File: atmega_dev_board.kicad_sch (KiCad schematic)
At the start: 40 parts, among them J1 GPIO Header, J2 USB_B_Micro, J3 GPIO Header, J4 ICSP Header, Q1 Q_PMOS_DGS, SW1 SW_Push, U1 LM358, U2 NCV8114ASN330T1G, U3 NCV8114ASN330T1G, U4 ATmega328P-A, U5 CH340G, Y1 Crystal_GND23, Y2 Crystal_GND23

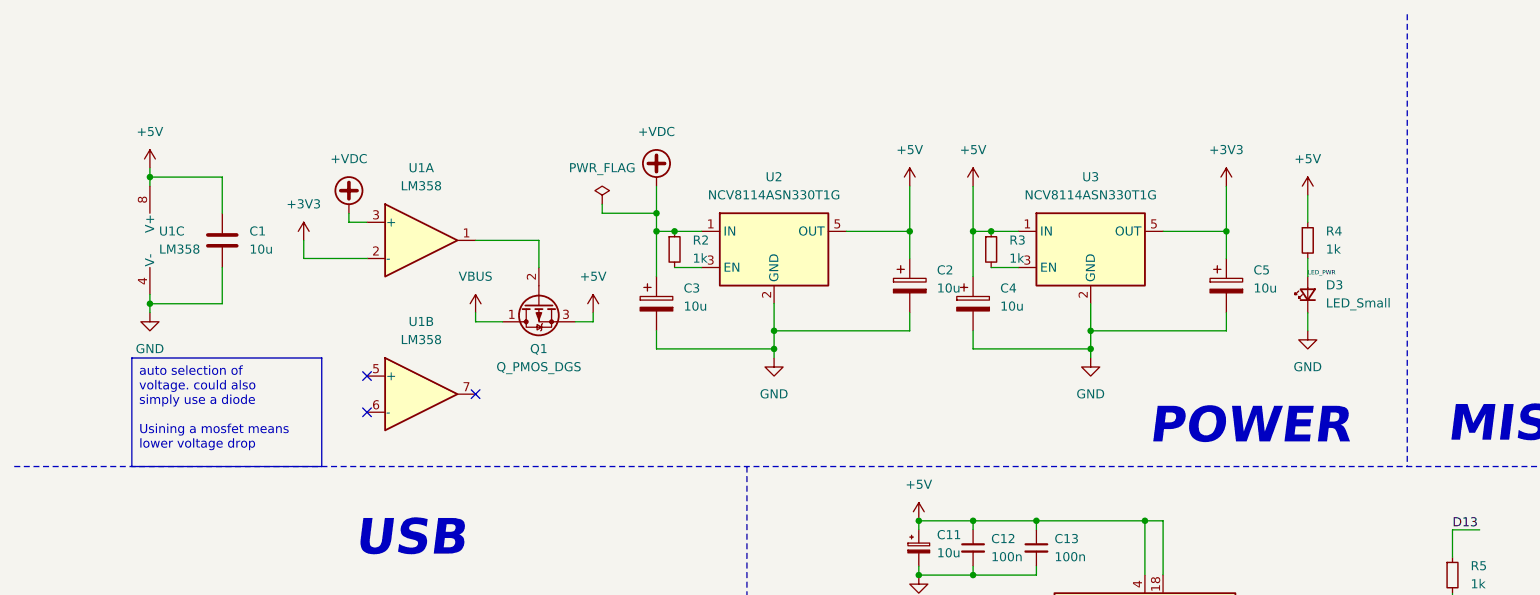
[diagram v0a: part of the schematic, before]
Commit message: Replace op-amps with a diode
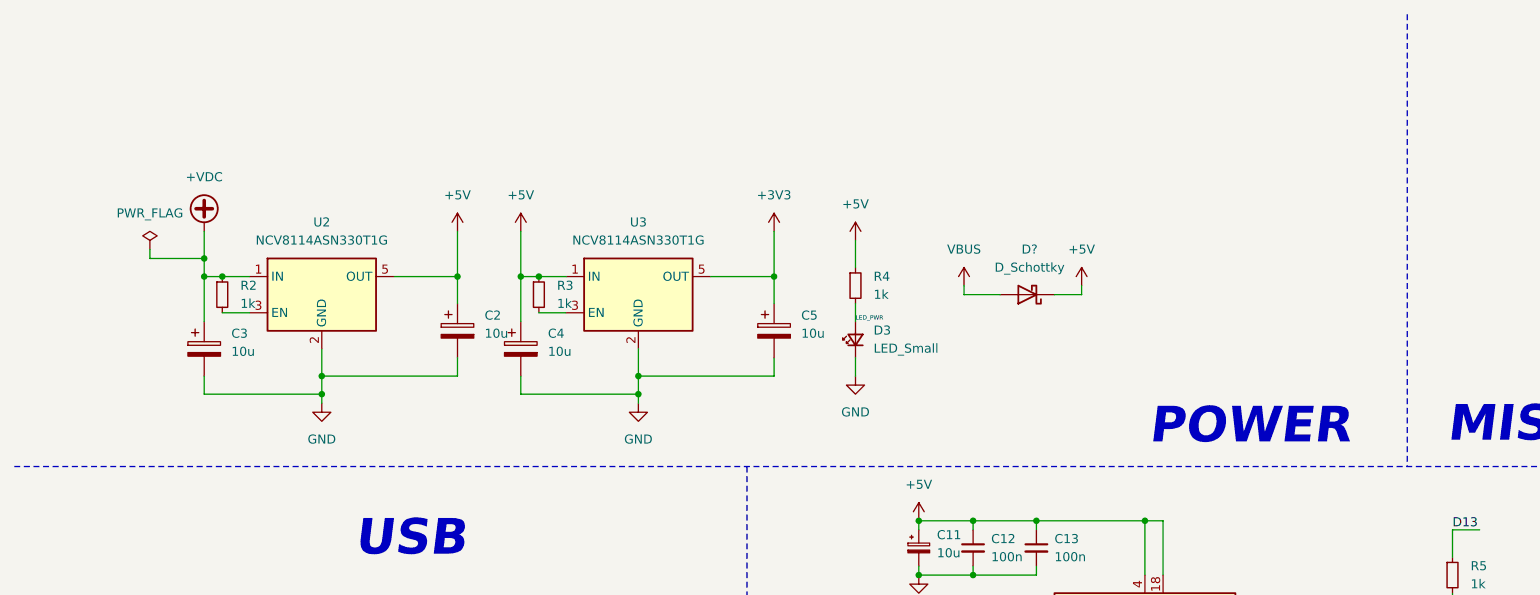
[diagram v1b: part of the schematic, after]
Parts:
- removed C1: 10u, Capacitor_SMD:C_0603_1608Metric, symbol Device:C
- removed Q1: Q_PMOS_DGS, Package_TO_SOT_SMD:SOT-23, symbol Device:Q_PMOS_DGS
- removed U1: LM358, Package_SO:SOIC-8_3.9x4.9mm_P1.27mm, symbol Amplifier_Operational:LM358
- added D?: D_Schottky, symbol Device:D_Schottky
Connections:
- net +5V: now also D?.1 (K)
- net VBUS: now also D?.2 (A)
- no-connect marks 12 -> 9
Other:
- moved on the sheet: C2, C3, C4, C5, D3, R2, R3, R4, U2, U3

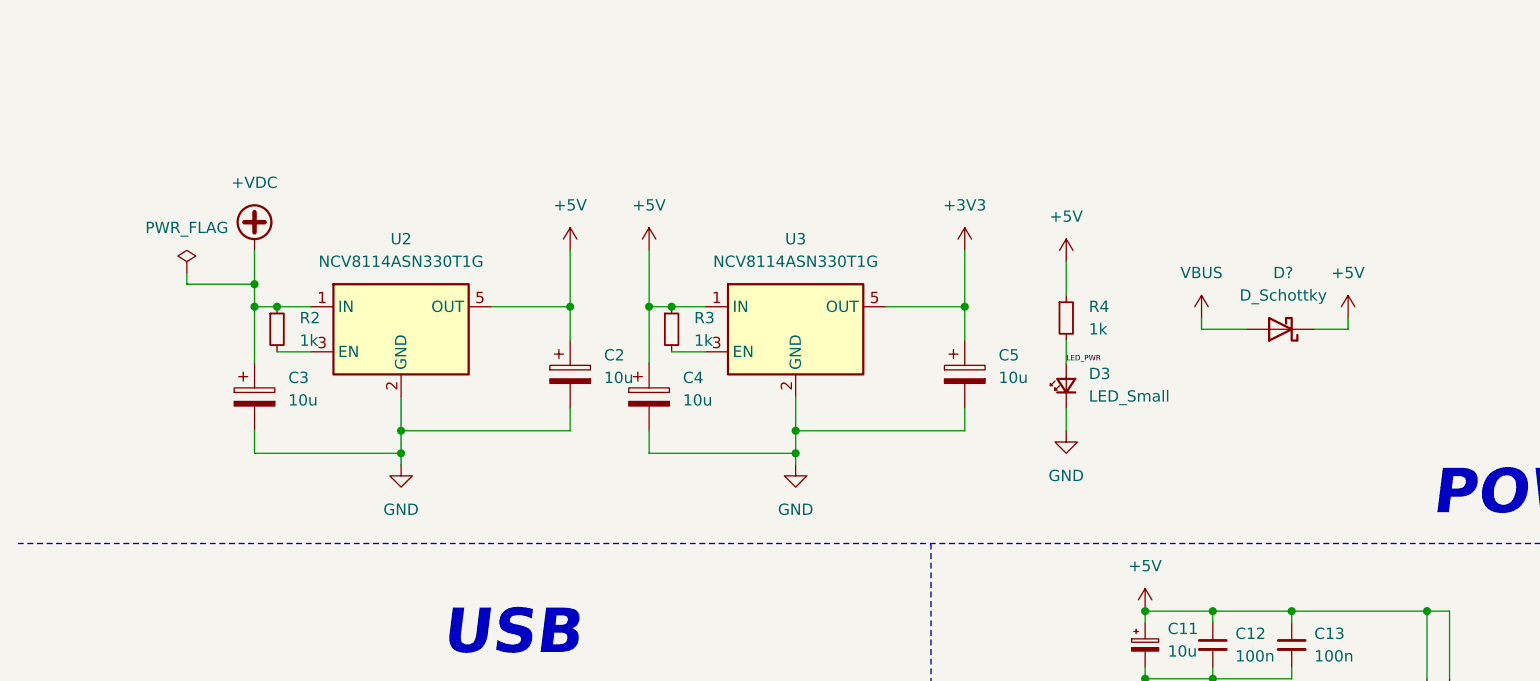
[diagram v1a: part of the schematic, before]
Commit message: Replace voltage regulators with 78XXs
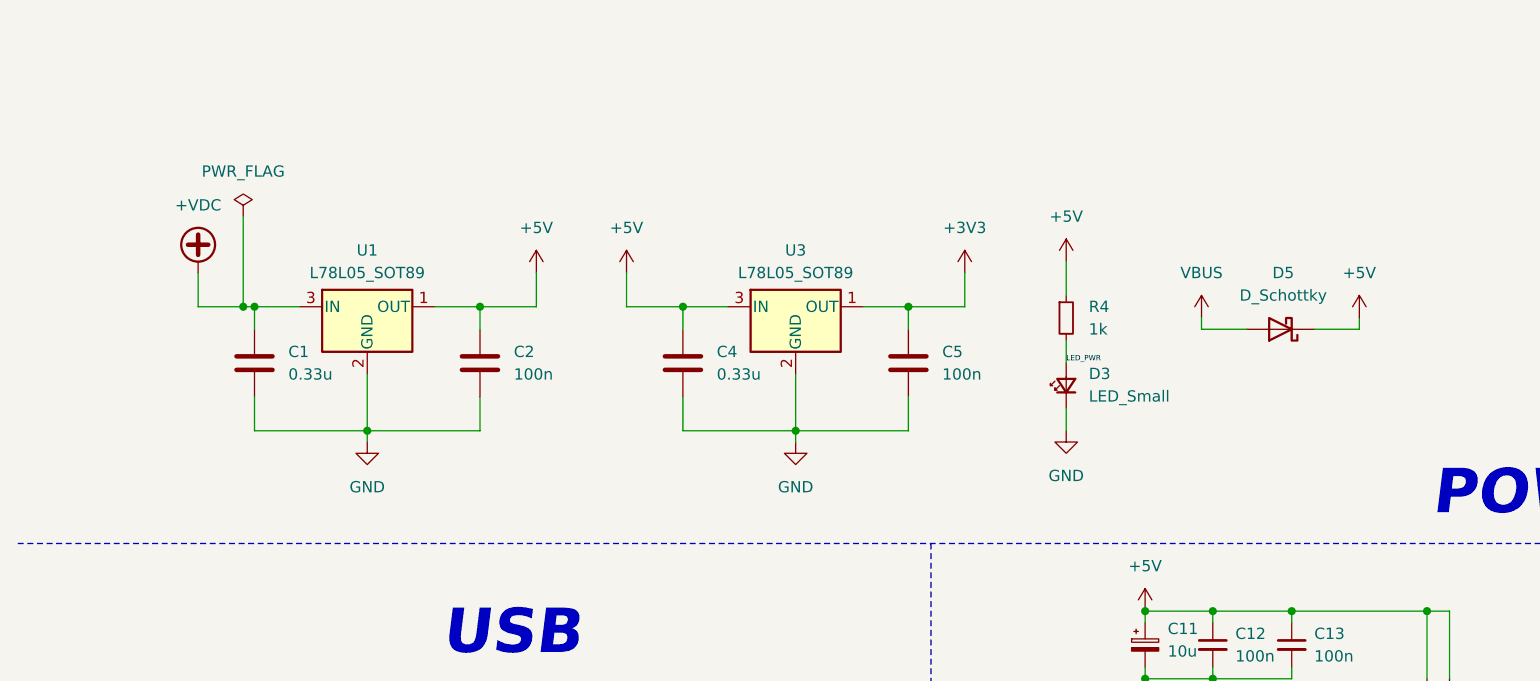
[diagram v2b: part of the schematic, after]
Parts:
- removed C2, C3: 10u, Capacitor_SMD:C_0603_1608Metric, symbol Device:C_Polarized
- removed R2, R3: 1k, Resistor_SMD:R_0603_1608Metric, symbol Device:R_Small
- removed U2: NCV8114ASN330T1G, Package_SO:TSOP-5_1.65x3.05mm_P0.95mm, symbol Regulator_Linear:NCV8114ASN330T1G
- added C1: 0.33u, Capacitor_SMD:C_0603_1608Metric, symbol Device:C
- added C2: 100n, Capacitor_SMD:C_0603_1608Metric, symbol Device:C
- added U1: L78L05_SOT89, Package_TO_SOT_SMD:SOT-89-3, symbol Regulator_Linear:L78L05_SOT89
- C4: value 10u -> 0.33u; symbol Device:C_Polarized -> Device:C
- C5: value 10u -> 100n; symbol Device:C_Polarized -> Device:C
- U3: value NCV8114ASN330T1G -> L78L05_SOT89; footprint Package_SO:TSOP-5_1.65x3.05mm_P0.95mm -> Package_TO_SOT_SMD:SOT-89-3; symbol Regulator_Linear:NCV8114ASN330T1G -> Regulator_Linear:L78L05_SOT89
- gave numbers to parts that had none: 1
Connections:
- net +3V3: now also U3.1 (OUT); no longer U3.5 (OUT)
- net +5V: now also U3.3 (IN), C2.1, U1.1 (OUT); no longer U3.1 (IN)
- net +VDC: now also C1.1, U1.3 (IN)
- net GND: now also C1.2, C2.2, U1.2 (GND)

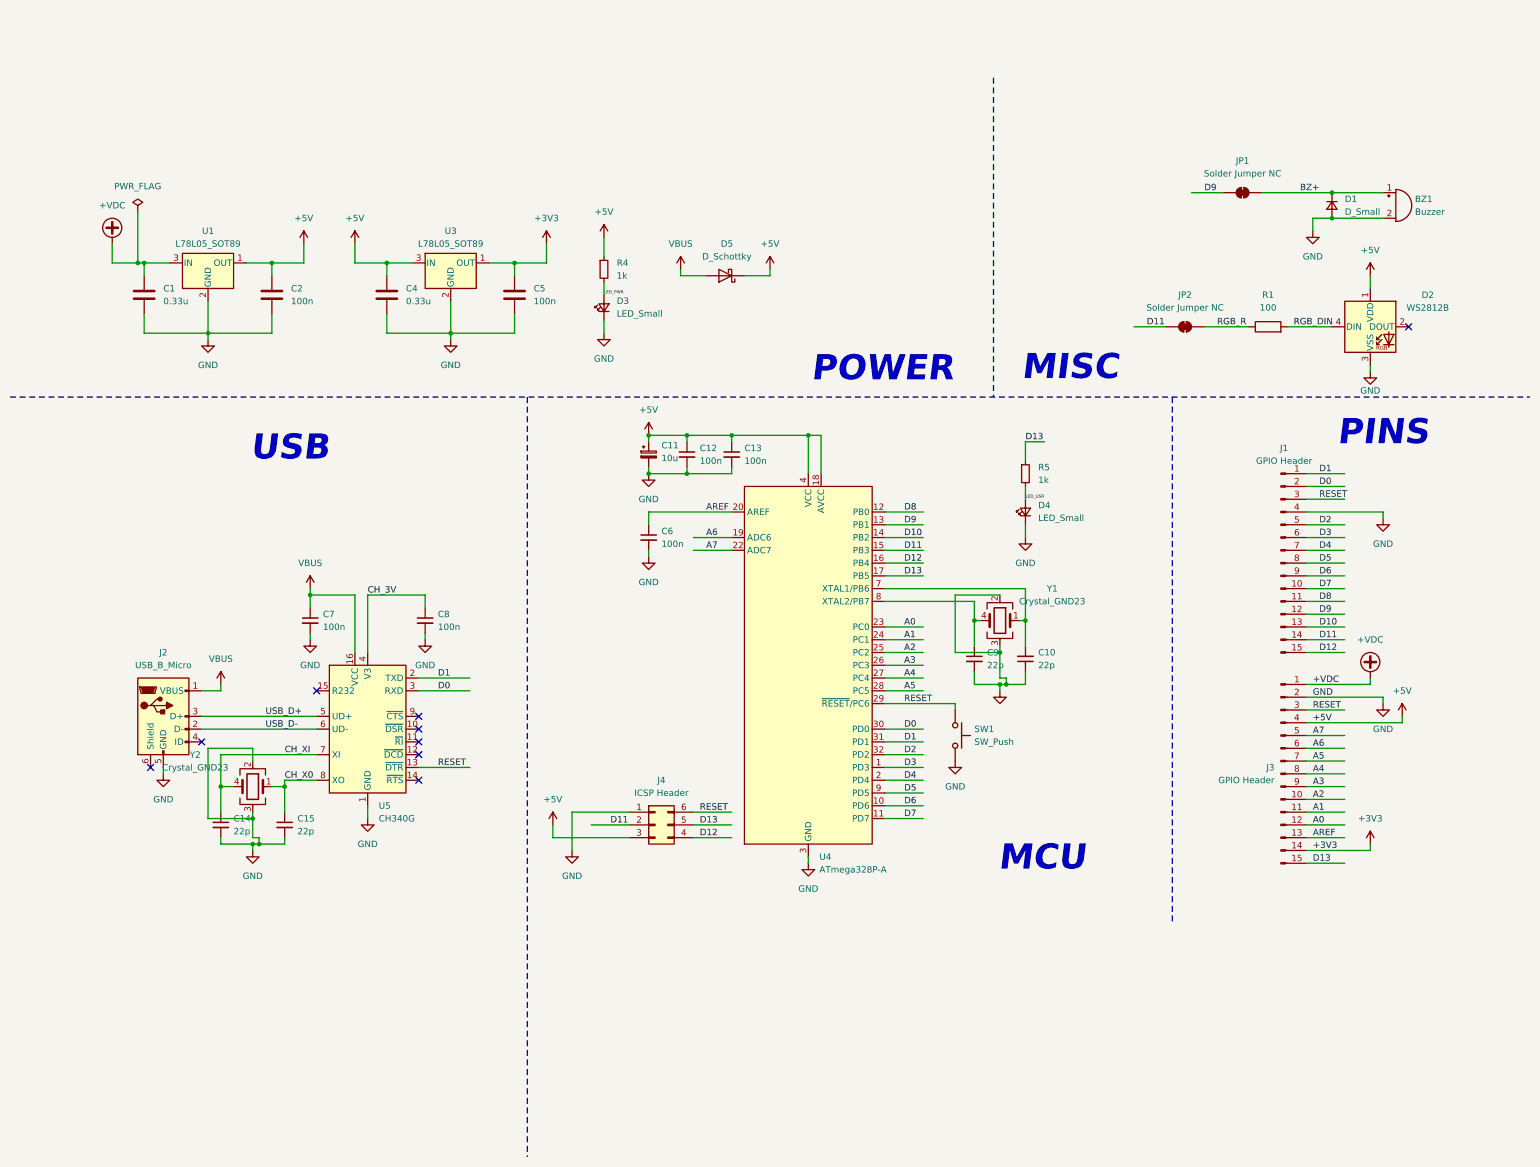
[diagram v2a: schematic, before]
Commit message: Move to USB C and CP2102
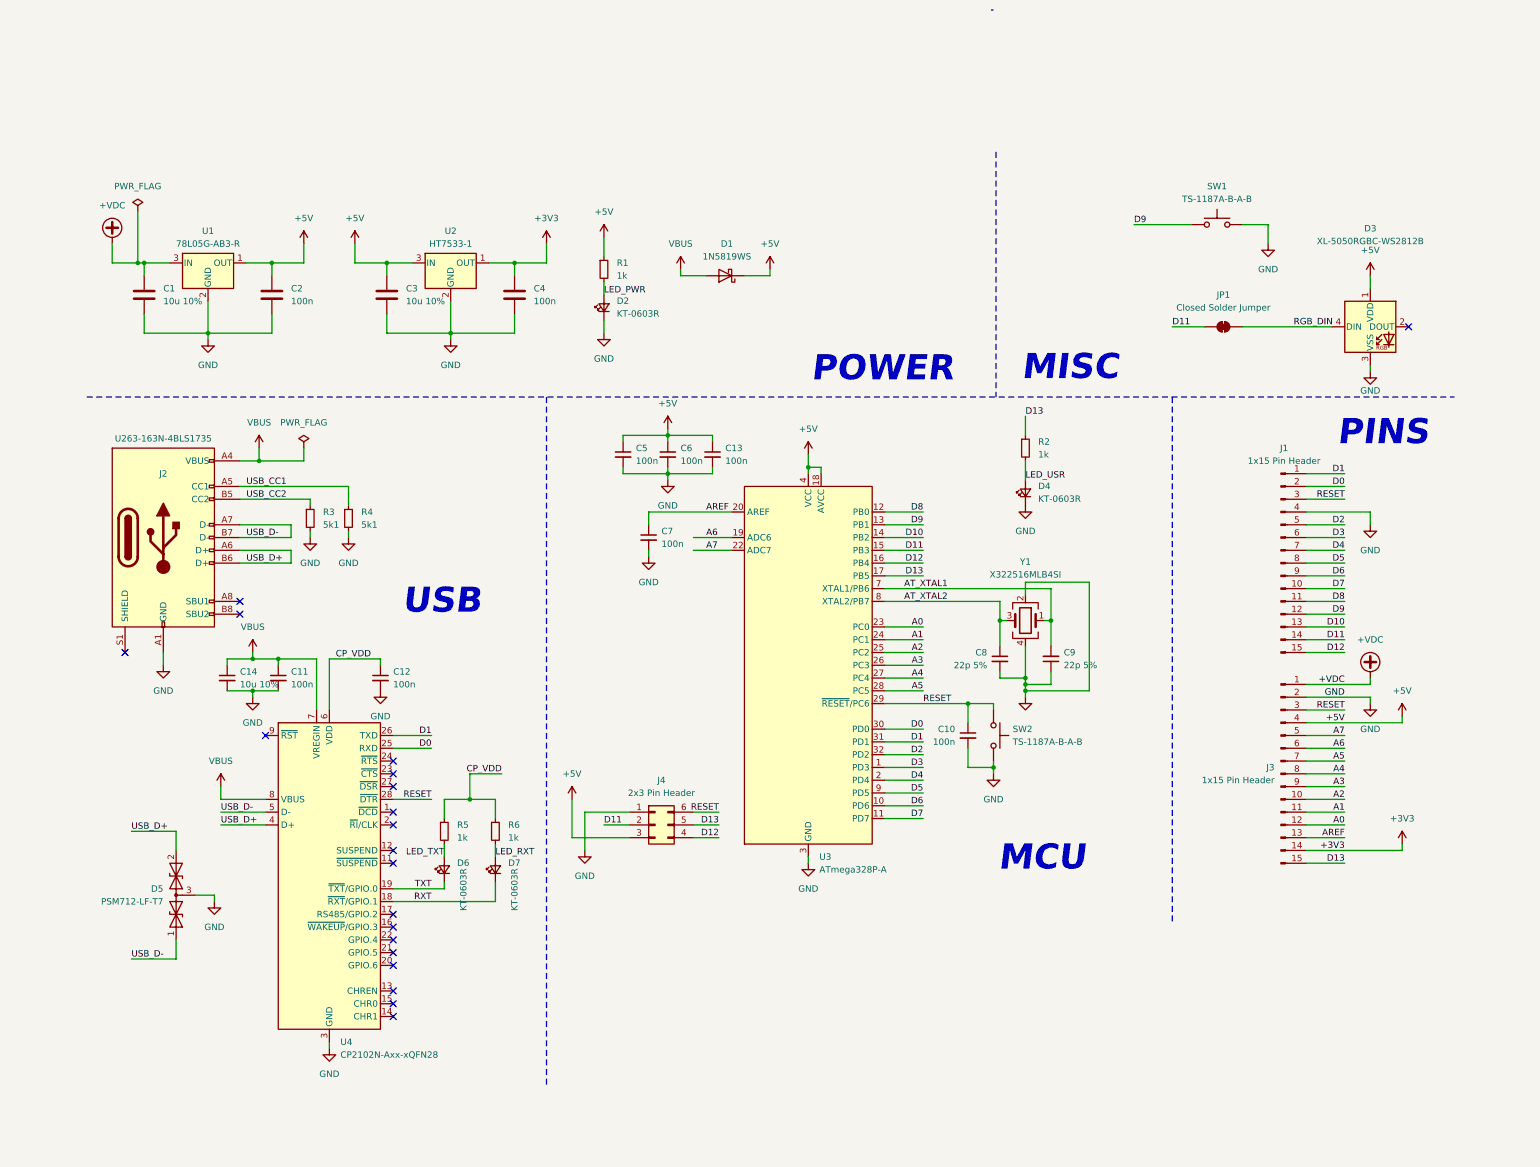
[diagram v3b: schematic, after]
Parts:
- removed BZ1: Buzzer, Buzzer_Beeper:Buzzer_Murata_PKMCS0909E, symbol Device:Buzzer
- removed C11: 10u, Capacitor_SMD:C_0603_1608Metric, symbol Device:C_Polarized_Small
- removed C15: 22p, Capacitor_SMD:C_0603_1608Metric, symbol Device:C_Small
- removed C7, C8: 100n, Capacitor_SMD:C_0603_1608Metric, symbol Device:C_Small
- removed D1: D_Small, Diode_SMD:D_0603_1608Metric, symbol Device:D_Small
- removed JP1: Solder Jumper NC, Jumper:SolderJumper-2_P1.3mm_Bridged_RoundedPad1.0x1.5mm, symbol Jumper:SolderJumper_2_Bridged
- removed R1: 100, Resistor_SMD:R_0603_1608Metric, symbol Device:R
- removed U5: CH340G, Package_SO:SOIC-16_3.9x9.9mm_P1.27mm, symbol Interface_USB:CH340G
- removed Y2: Crystal_GND23, Crystal:Crystal_SMD_3225-4Pin_3.2x2.5mm, symbol Device:Crystal_GND23
- added C10, C11, C12, C13: 100n, Capacitor_SMD:C_0603_1608Metric, symbol Device:C_Small
- added D5: PSM712-LF-T7, Package_TO_SOT_SMD:SOT-23, symbol Diode:SM712_SOT23
- added D6, D7: KT-0603R, LED_SMD:LED_0603_1608Metric, symbol Device:LED_Small
- added R3, R4: 5k1, Resistor_SMD:R_0603_1608Metric, symbol Device:R_Small
- added R5, R6: 1k, Resistor_SMD:R_0603_1608Metric, symbol Device:R_Small
- added SW1: TS-1187A-B-A-B, Button_Switch_SMD:SW_SPST_TL3342, symbol Switch:SW_Push
- added U4: CP2102N-Axx-xQFN28, Package_DFN_QFN:QFN-28-1EP_5x5mm_P0.5mm_EP3.35x3.35mm, symbol Interface_USB:CP2102N-Axx-xQFN28
- C1: value 0.33u -> 10u 10%; JLCPCB Part# (none) -> C19702
- C14: value 22p -> 10u 10%; JLCPCB Part# (none) -> C19702
- C2: JLCPCB Part# (none) -> C14663
- C3: renamed from C4; value 0.33u -> 10u 10%; JLCPCB Part# (none) -> C19702
- C4: renamed from C5; JLCPCB Part# (none) -> C14663
- C5: renamed from C12; JLCPCB Part# (none) -> C14663
- C6: renamed from C13; JLCPCB Part# (none) -> C14663
- C7: renamed from C6; JLCPCB Part# (none) -> C14663
- C8: renamed from C9; value 22p -> 22p 5%; JLCPCB Part# (none) -> C2991405
- C9: renamed from C10; value 22p -> 22p 5%; JLCPCB Part# (none) -> C2991405
- D1: renamed from D5; value D_Schottky -> 1N5819WS; footprint (none) -> Diode_SMD:D_SOD-323; JLCPCB Part# (none) -> C191023
- D2: renamed from D3; value LED_Small -> KT-0603R; JLCPCB Part# (none) -> C2286
- D3: renamed from D2; value WS2812B -> XL-5050RGBC-WS2812B; JLCPCB Part# (none) -> C2843785
- D4: value LED_Small -> KT-0603R; JLCPCB Part# (none) -> C2286
- J1, J3: value GPIO Header -> 1x15 Pin Header
- J2: value USB_B_Micro -> U263-163N-4BLS1735; footprint Connector_USB:USB_Micro-B_Molex_47346-0001 -> Connector_USB:USB_C_Receptacle_GCT_USB4105-xx-A_16P_TopMnt_Horizontal; symbol Connector:USB_B_Micro -> Connector:USB_C_Receptacle_USB2.0_16P; JLCPCB Part# (none) -> C2931474
- J4: value ICSP Header -> 2x3 Pin Header
- JP1: renamed from JP2; value Solder Jumper NC -> Closed Solder Jumper
- R1: renamed from R4; JLCPCB Part# (none) -> C21190
- R2: renamed from R5; JLCPCB Part# (none) -> C21190
- SW2: renamed from SW1; value SW_Push -> TS-1187A-B-A-B; footprint Button_Switch_SMD:SW_SPST_B3U-1000P -> Button_Switch_SMD:SW_SPST_TL3342; JLCPCB Part# (none) -> C318884
- U1: value L78L05_SOT89 -> 78L05G-AB3-R; JLCPCB Part# (none) -> C71136
- U2: renamed from U3; value L78L05_SOT89 -> HT7533-1; symbol Regulator_Linear:L78L05_SOT89 -> Regulator_Linear:L78L33_SOT89; JLCPCB Part# (none) -> C14289
- U3: renamed from U4; JLCPCB Part# (none) -> C14877
- Y1: value Crystal_GND23 -> X322516MLB4SI; symbol Device:Crystal_GND23 -> Device:Crystal_GND24; JLCPCB Part# (none) -> C13738
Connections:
- net CH_XI is gone; now on net VBUS: C14.1
- net RGB_R is gone; now on net RGB_DIN: JP1.2 (B)
- net +5V: now also C13.1
- net D0: now also U4.25 (RXD)
- net D1: now also U4.26 (TXD)
- net D9: now also SW1.1
- net GND: now also J2.A1 (GND), J2.A12 (GND), J2.B1 (GND), J2.B12 (GND), Y1.4, C10.2, C11.2, C12.2, C13.2, D5.3 (common), R3.2, R4.2, SW1.2, U4.29 (GND), U4.3 (GND); no longer J2.5 (GND), Y1.3
- net RESET: now also C10.1, U4.28 (~{DTR})
- net USB_D+: now also J2.A6 (D+), J2.B6 (D+), D5.2 (A2), U4.4 (D+); no longer J2.3 (D+)
- net USB_D-: now also J2.A7 (D-), J2.B7 (D-), D5.1 (A1), U4.5 (D-); no longer J2.2 (D-)
- net VBUS: now also J2.A4 (VBUS), J2.A9 (VBUS), J2.B4 (VBUS), J2.B9 (VBUS), C11.1, U4.7 (VREGIN), U4.8 (VBUS); no longer J2.1 (VBUS)
- net AT_XTAL2: now reaches C8.1, U3.8 (XTAL2/PB7)
- net AT_XTAL2: now also Y1.3; no longer Y1.4
- net AT_XTAL1: now reaches C9.2, U3.7 (XTAL1/PB6), Y1.1
- new net CP_VDD: C12.1, R5.1, R6.1, U4.6 (VDD)
- new net LED_RXT: D7.2 (A), R6.2
- new net LED_TXT: D6.2 (A), R5.2
- new net RXT: D7.1 (K), U4.18 (~{RXT}/GPIO.1)
- new net TXT: D6.1 (K), U4.19 (~{TXT}/GPIO.0)
- new net USB_CC1: J2.A5 (CC1), R4.1
- new net USB_CC2: J2.B5 (CC2), R3.1
- no-connect marks 9 -> 20
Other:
- title: (none) -> Arduino Dolly
- moved on the sheet: C5, C6, C8, C9, D4, JP1, R2, SW2, Y1
